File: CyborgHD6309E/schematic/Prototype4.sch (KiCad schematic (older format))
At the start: 22 parts, among them J1 Conn_I2C_Master, J2 Conn_Micro_SD, J3 Conn_USB_Serial, J4 Conn_AVR_UPDI, J5 Conn_AVR_UPDI, SW1 USR_SW, U1 ATmega4809-P, U2 HM628128DLP-5, U3 HD63C09E, U4 ATtiny416-S

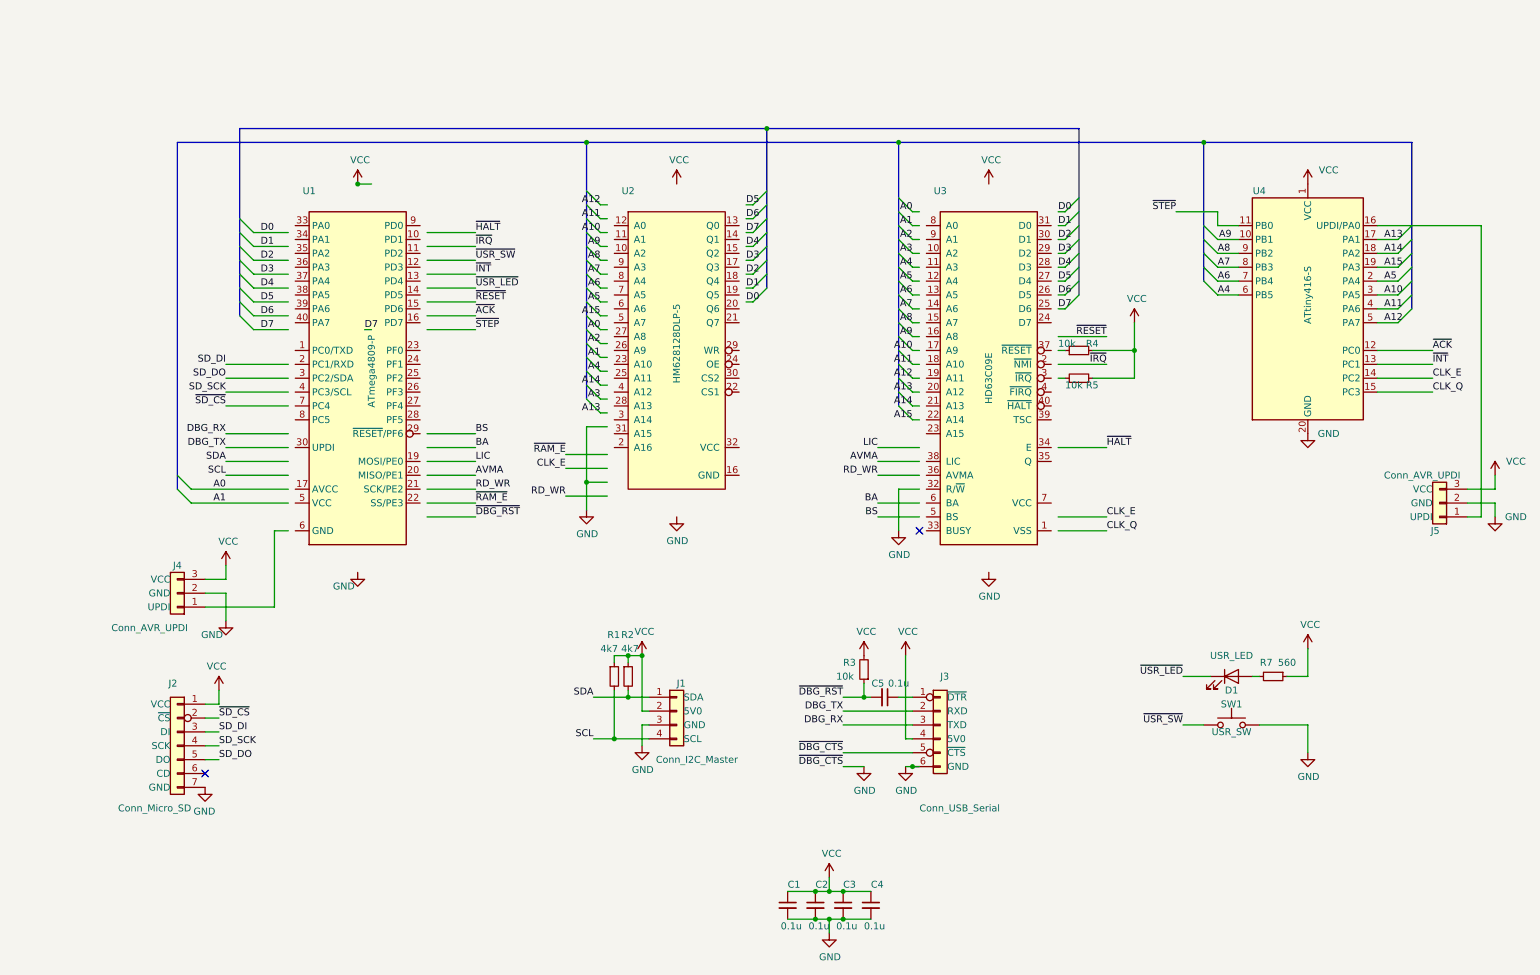
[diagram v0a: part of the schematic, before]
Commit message: [HD6309E] Use ATtiny414 + 7430 + 74688 for clock generator
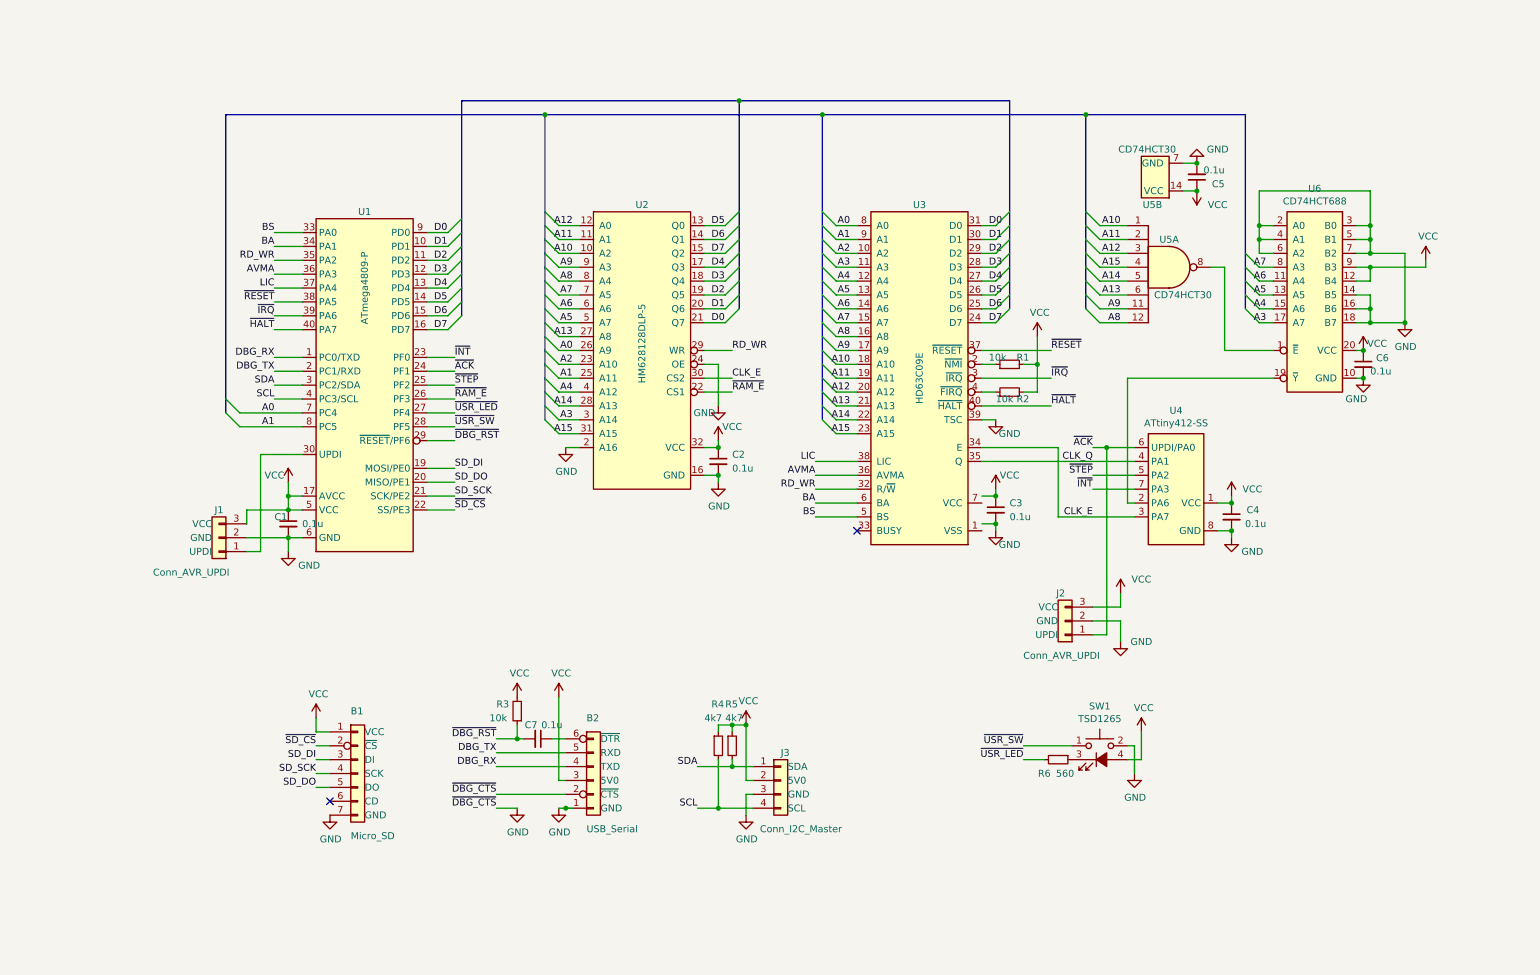
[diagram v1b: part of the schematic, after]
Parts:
- removed D1: USR_LED, LED_THT:LED_D3.0mm, symbol Device:LED
- removed J2: Conn_Micro_SD, Connector_PinSocket_2.54mm:PinSocket_1x07_P2.54mm_Vertical, symbol 0-LocalLibrary:Conn_Micro_SD
- removed J3: Conn_USB_Serial, Connector_PinSocket_2.54mm:PinSocket_1x06_P2.54mm_Vertical, symbol 0-LocalLibrary:Conn_USB_Serial
- removed SW1: USR_SW, Button_Switch_THT:SW_PUSH_6mm_H5mm, symbol Switch:SW_Push
- removed U4: ATtiny416-S, Package_DIP:DIP-20_W7.62mm, symbol 0-LocalLibrary:ATtiny416-S
- added B1: Micro_SD, 0-LocalLibrary:uSD_CARD, symbol 0-LocalLibrary:Micro_SD
- added B2: USB_Serial, 0-LocalLibrary:GY232V2, symbol 0-LocalLibrary:USB_Serial
- added C5, C6: 0.1u, Capacitor_THT:C_Disc_D3.4mm_W2.1mm_P2.50mm, symbol Device:C_Small
- added SW1: TSD1265, 0-LocalLibrary:SW_PUSH-LED-12mm, symbol 0-LocalLibrary:SW_Push_LED
- added U4: ATtiny412-SS, Package_DIP:DIP-8_W7.62mm, symbol 0-LocalLibrary:ATtiny412-SS
- added U5: CD74HCT30, Package_DIP:DIP-14_W7.62mm, symbol 0-LocalLibrary:74HC30
- added U6: CD74HCT688, Package_DIP:DIP-20_W7.62mm, symbol 0-LocalLibrary:CD74HCT688
- renumbered C5 to C7, J4 to J1, J5 to J2, J1 to J3, R4 to R1, R5 to R2, R1 to R4, R2 to R5, R7 to R6
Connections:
- wire segments 190 -> 227
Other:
- moved on the sheet: C1, C2, C3, C4, C7, J1, J2, J3, R1, R2, R3, R4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

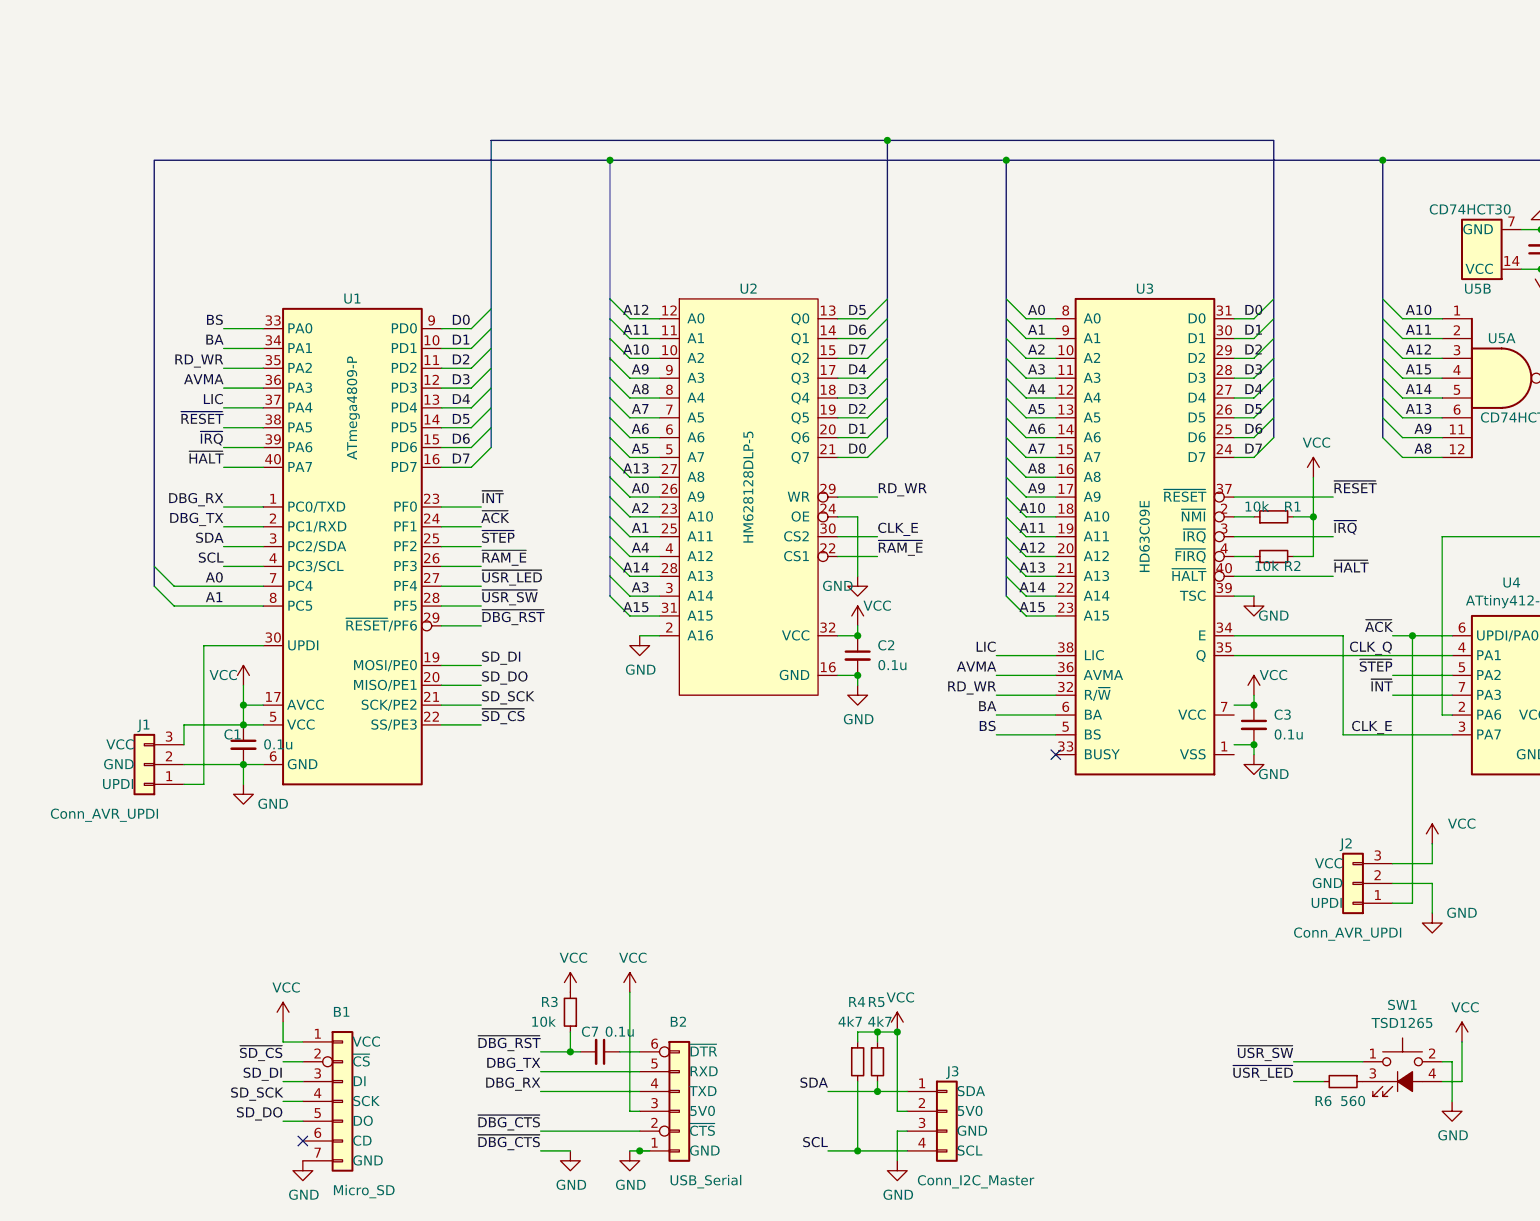
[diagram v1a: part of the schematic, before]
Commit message: [CyborgHD6309E] Update pin_maps.h and schematics
- Add DBG_RTS for hard flowcontrol of console.
- Use port A for data bus and port D for controls.
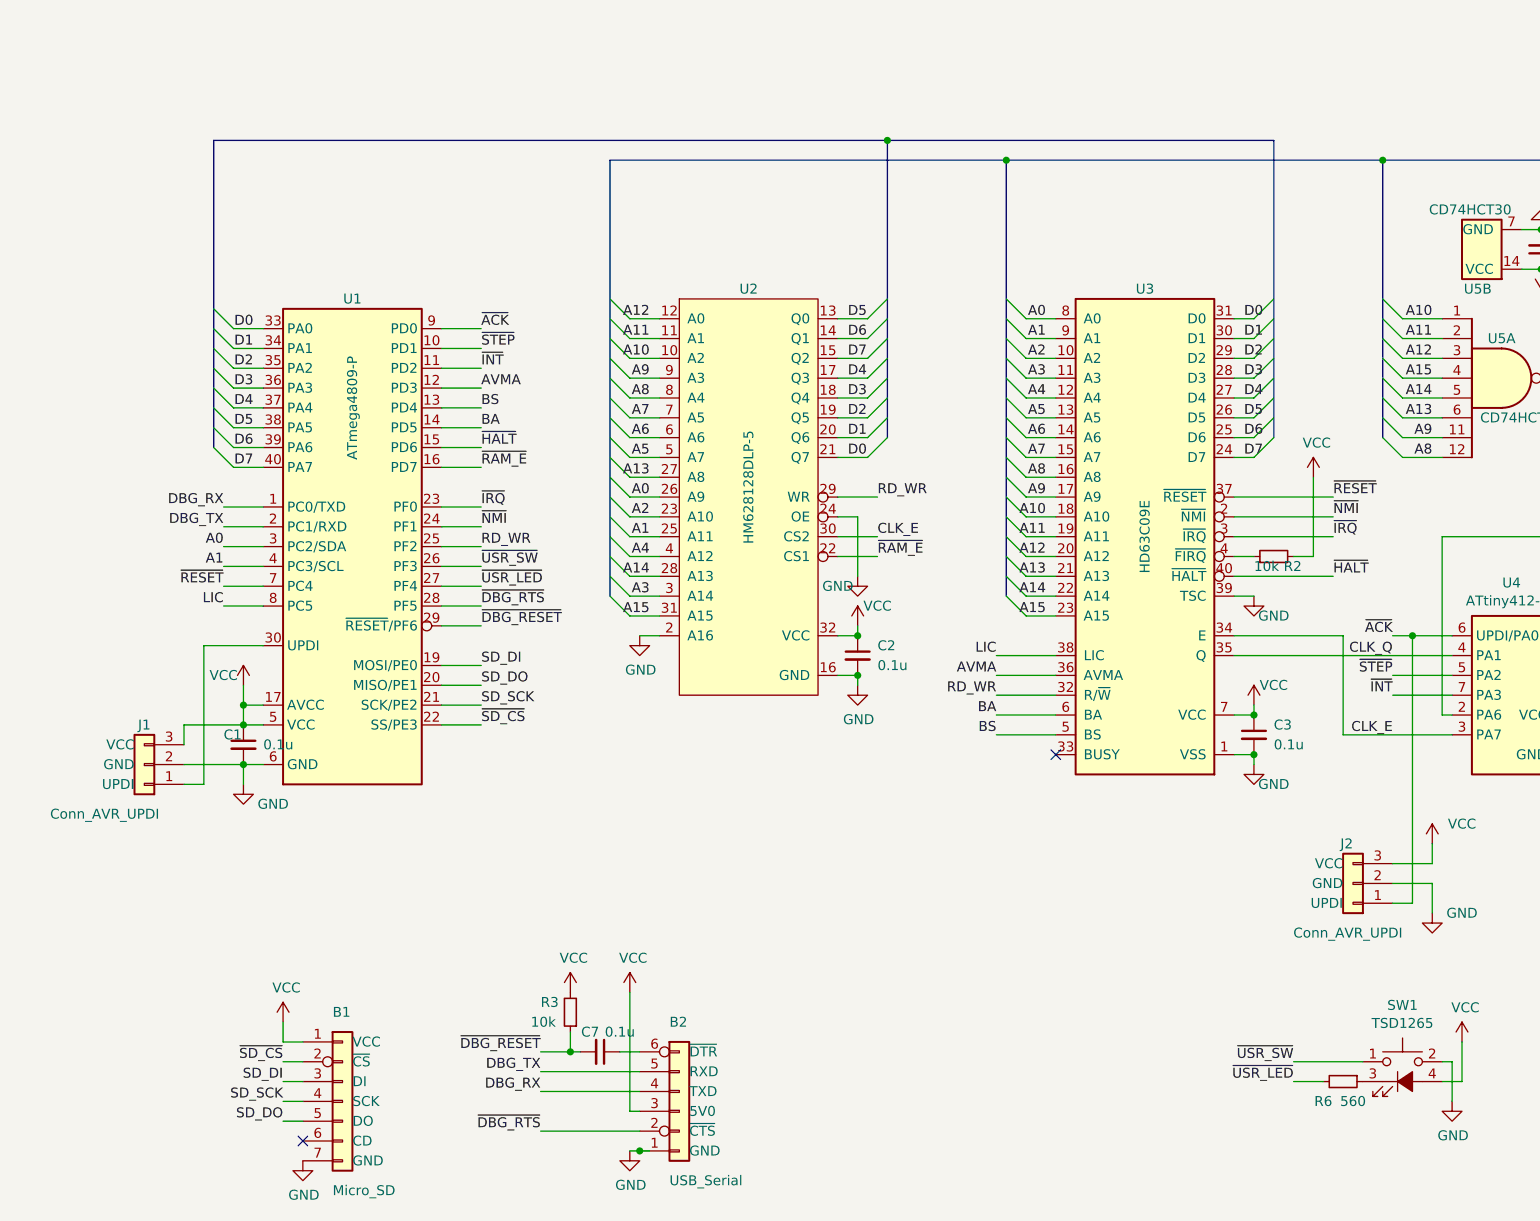
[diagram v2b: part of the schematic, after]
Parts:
- removed J3: Conn_I2C_Master, Connector_PinSocket_2.54mm:PinSocket_1x04_P2.54mm_Vertical, symbol 0-LocalLibrary:Conn_I2C_Master
- removed R1: 10k, Resistor_THT:R_Axial_DIN0204_L3.6mm_D1.6mm_P5.08mm_Horizontal, symbol Device:R_Small
- removed R4, R5: 4k7, Resistor_THT:R_Axial_DIN0204_L3.6mm_D1.6mm_P5.08mm_Horizontal, symbol Device:R_Small
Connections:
- net SCL is gone; now on net A1: U1.4 (PC3/SCL)
- net SDA is gone; now on net A0: U1.3 (PC2/SDA)
- net A0: no longer U1.7 (PC4)
- net A1: no longer U1.8 (PC5)
- net AVMA: now also U1.12 (PD3); no longer U1.36 (PA3)
- net BA: now also U1.14 (PD5); no longer U1.34 (PA1)
- net BS: now also U1.13 (PD4); no longer U1.33 (PA0)
- net D0: now also U1.33 (PA0); no longer U1.9 (PD0)
- net D1: now also U1.34 (PA1); no longer U1.10 (PD1)
- net D2: now also U1.35 (PA2); no longer U1.11 (PD2)
- net D3: now also U1.36 (PA3); no longer U1.12 (PD3)
- net D4: now also U1.37 (PA4); no longer U1.13 (PD4)
- net D5: now also U1.38 (PA5); no longer U1.14 (PD5)
- net D6: now also U1.39 (PA6); no longer U1.15 (PD6)
- net D7: now also U1.40 (PA7); no longer U1.16 (PD7)
- net GND: now also U3.1 (VSS); no longer B2.2 (~CTS~)
- net LIC: now also U1.8 (PC5); no longer U1.37 (PA4)
- net RD_WR: now also U1.25 (PF2); no longer U1.35 (PA2)
- net VCC: now also U3.7 (VCC)
- net ~USR_SW~: now also U1.26 (PF3); no longer U1.28 (PF5)
- net ~NMI~: now reaches U3.2 (~NMI)
- net ~NMI~: now also U1.24 (PF1)
- net ~ACK renamed ~ACK~
- net ~ACK~: now also U1.9 (PD0); no longer U1.24 (PF1)
- net ~DBG_RST~ renamed ~DBG_RESET~
- net ~HALT renamed ~HALT~
- net ~HALT~: now also U1.15 (PD6); no longer U1.40 (PA7)
- net ~INT renamed ~INT~
- net ~INT~: now also U1.11 (PD2); no longer U1.23 (PF0)
- net ~IRQ renamed ~IRQ~
- net ~IRQ~: now also U1.23 (PF0); no longer U1.39 (PA6)
- net ~RAM_E renamed ~RAM_E~
- net ~RAM_E~: now also U1.16 (PD7); no longer U1.26 (PF3)
- net ~RESET renamed ~RESET~
- net ~RESET~: now also U1.7 (PC4); no longer U1.38 (PA5)
- net ~SD_CS renamed ~SD_CS~
- net ~STEP renamed ~STEP~
- net ~STEP~: now also U1.10 (PD1); no longer U1.25 (PF2)
- new net ~DBG_RTS~: B2.2 (~CTS~), U1.28 (PF5)
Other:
- moved on the sheet: C3
